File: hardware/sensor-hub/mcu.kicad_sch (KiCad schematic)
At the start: 44 parts, among them J1 Conn_ARM_JTAG_SWD_10, J2 Micro_SD_Card_Det2, SW1 SW_Push, U1 STM32F411CEUx, U4 PCAL6408ABS, Y2 32.768kHz, Y3 16MHz

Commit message: Add sensors, connectors
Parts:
- removed TP1, TP3: TestPoint, symbol Connector:TestPoint
- added J8: Conn_01x03, symbol Connector_Generic:Conn_01x03
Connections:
- net GND: now also J8.3 (Pin_3)
- net USART2_RX: now also J8.2 (Pin_2)
- net USART2_TX: now also J8.1 (Pin_1)
- net RADIO_CE: now reaches U1.10 (PA0)
- net RADIO_IRQ: now reaches U1.27 (PB14)
- net I2C1_SCL renamed SCL
- net I2C1_SDA renamed SDA
- net SPI4_MISO renamed RADIO_MISO
- net SPI4_MOSI renamed RADIO_MOSI
- net SPI4_NSS renamed RADIO_CS
- net SPI4_SCK renamed RADIO_SCK

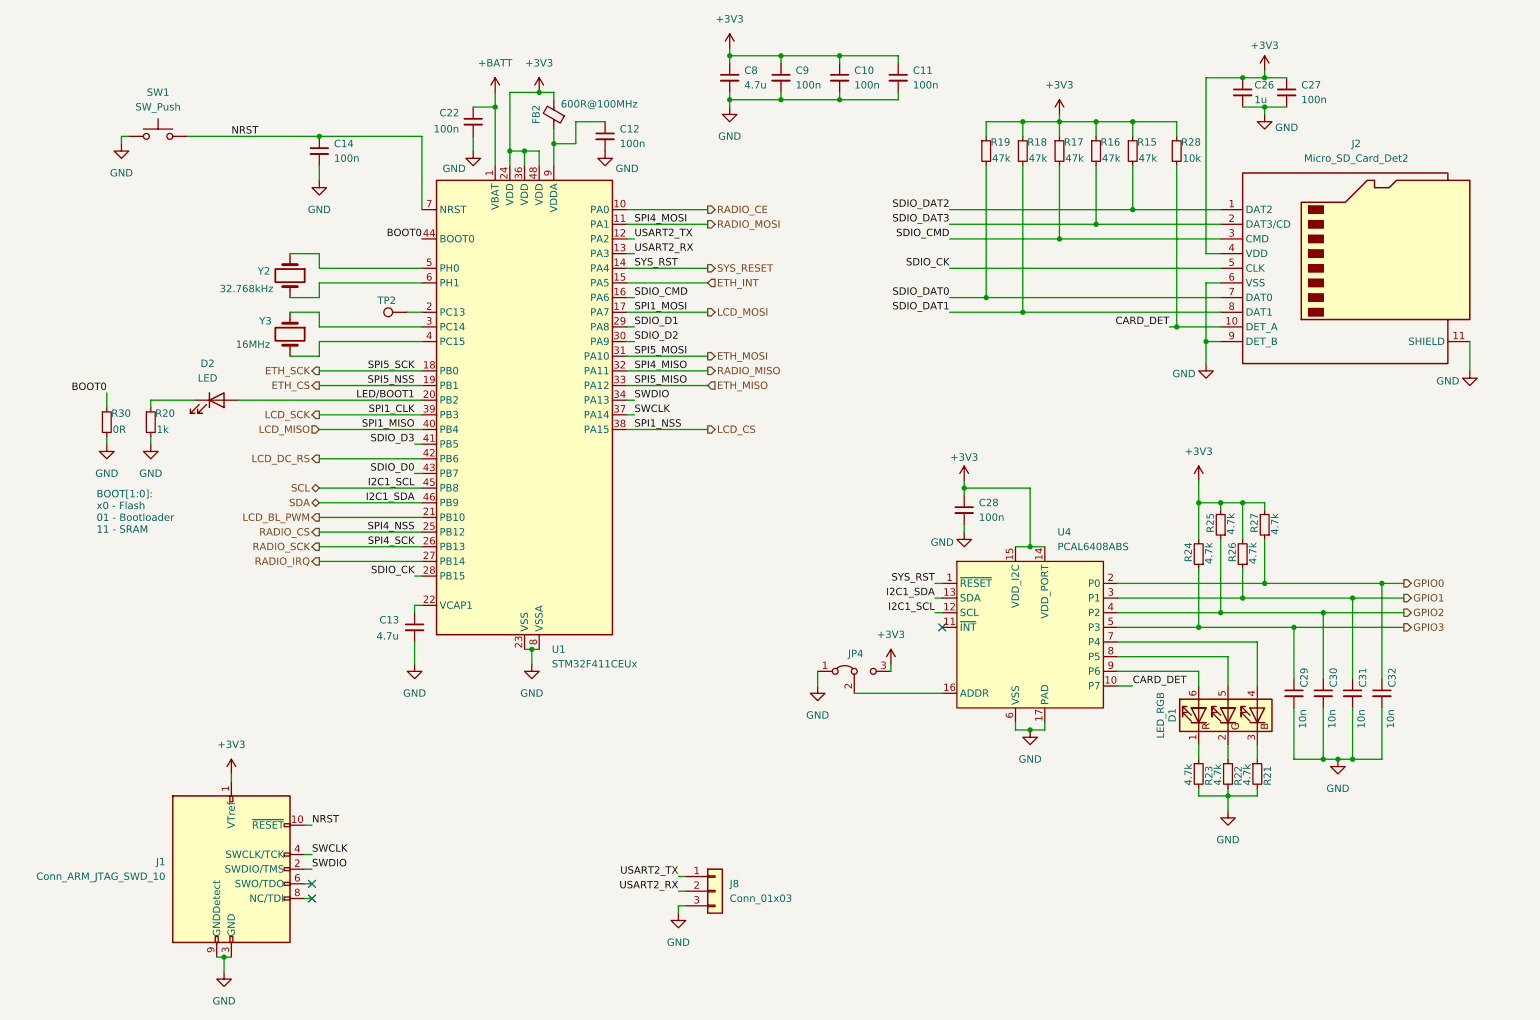
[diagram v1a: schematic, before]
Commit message: Change crystal packages, assign footprints
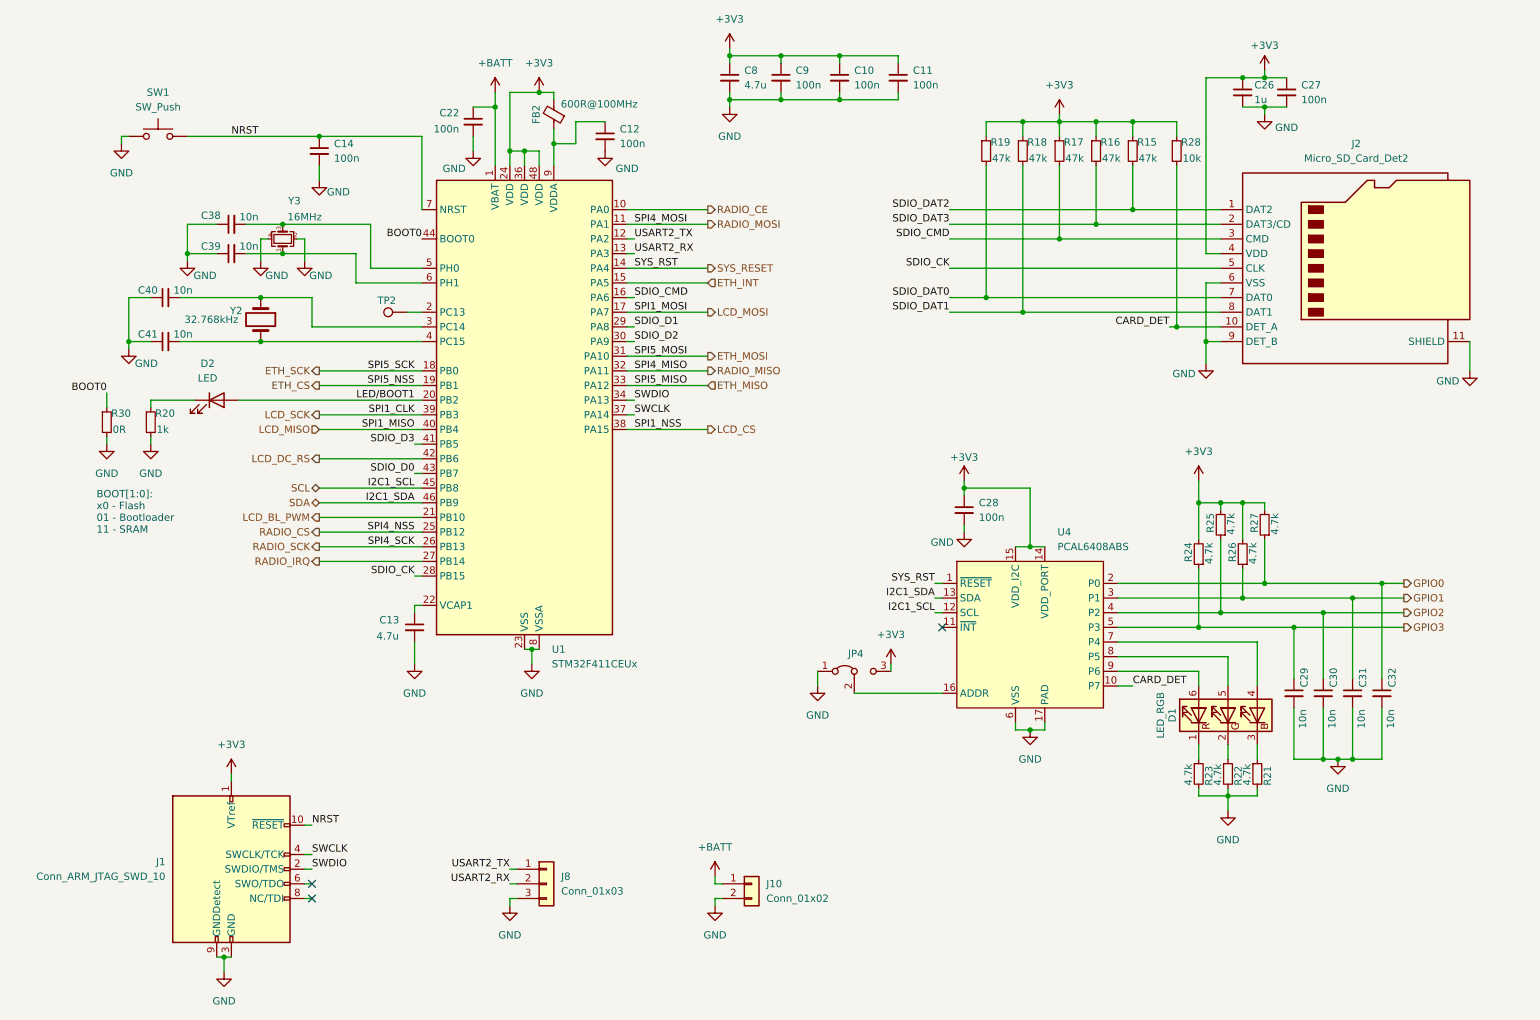
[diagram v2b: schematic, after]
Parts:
- removed Y3: 16MHz, symbol Device:Crystal
- added C38, C39, C40, C41: 10n, Capacitor_SMD:C_0603_1608Metric, symbol Device:C_Small
- added J10: Conn_01x02, Battery:BatteryHolder_MYOUNG_BS-07-A1BJ001_CR2032, symbol Connector_Generic:Conn_01x02
- added Y3: 16MHz, symbol Device:Crystal_GND24_Small
- C10, C11, C12, C13, C14, C22, C26, C27, C28, C29, C30, C31, C32, C8, C9: footprint (none) -> Capacitor_SMD:C_0603_1608Metric
- D2: footprint (none) -> LED_SMD:LED_0603_1608Metric
- FB2: footprint (none) -> Inductor_SMD:L_0603_1608Metric
- J1: footprint (none) -> Connector_PinHeader_1.27mm:PinHeader_2x05_P1.27mm_Vertical_SMD
- J2: footprint (none) -> sensor-hub-footprints:MicroSD_Det2
- J8: footprint (none) -> Connector_PinHeader_2.54mm:PinHeader_1x03_P2.54mm_Vertical
- JP4: footprint (none) -> Jumper:SolderJumper-3_P1.3mm_Bridged12_RoundedPad1.0x1.5mm
- R15, R16, R17, R18, R19, R20, R21, R22, R23, R24, R25, R26, R27, R28, R30: footprint (none) -> Resistor_SMD:R_0603_1608Metric
- SW1: footprint (none) -> Button_Switch_SMD:SW_SPST_CK_RS282G05A3
- TP2: footprint (none) -> TestPoint:TestPoint_Pad_D1.0mm
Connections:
- net +BATT: now also J10.1 (Pin_1)
- net GND: now also C38.1, C39.1, C40.1, C41.1, J10.2 (Pin_2), Y3.2, Y3.4
- net at U1.5 (PH0): now also C38.2, Y3.3; no longer Y2.1
- net at Y2.2: now also U1.4 (PC15), C41.2; no longer U1.6 (PH1)
- net at U1.3 (PC14): now also Y2.1, C40.2
- new net: C39.2, U1.6 (PH1), Y3.1
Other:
- moved on the sheet: J8, Y2

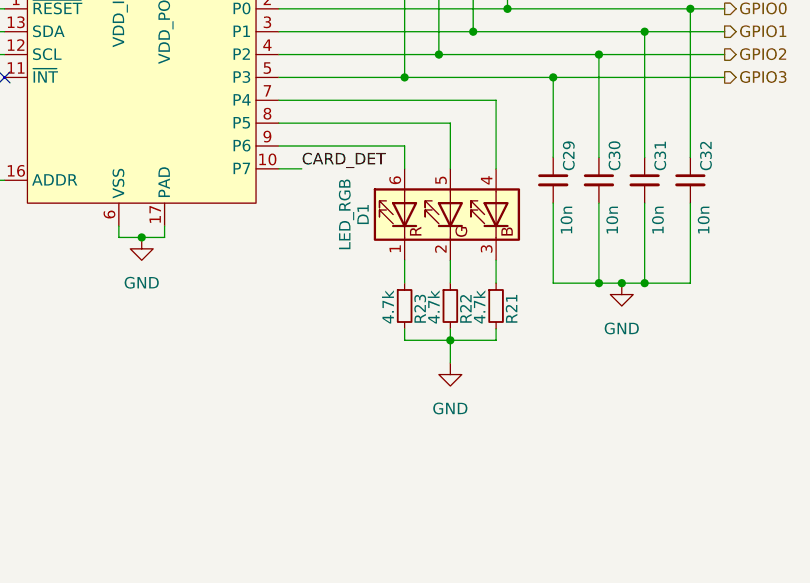
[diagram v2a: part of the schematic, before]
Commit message: Assign remaining footprints, change HT sensor
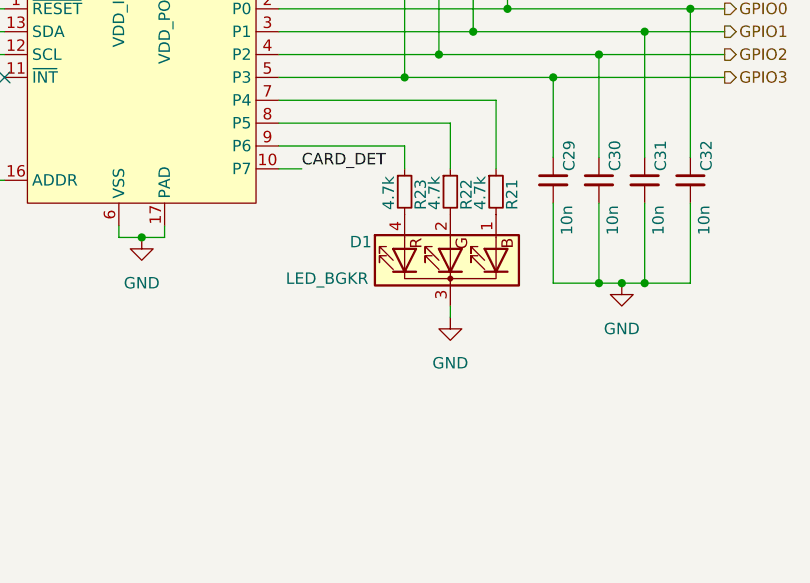
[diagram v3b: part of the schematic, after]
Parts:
- removed D1: LED_RGB, symbol Device:LED_RGB
- added D1: LED_BGKR, LED_SMD:LED_Cree-PLCC4_3.2x2.8mm_CCW, symbol Device:LED_BGKR
- Y2: footprint (none) -> Crystal:Crystal_SMD_3215-2Pin_3.2x1.5mm
- Y3: footprint (none) -> Crystal:Crystal_SMD_SeikoEpson_TSX3225-4Pin_3.2x2.5mm
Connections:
- net GND: now also D1.3 (K); no longer R21.2, R22.2, R23.2
- net at U4.7 (P4): now also R21.1
- net at U4.8 (P5): now also R22.1
- net at U4.9 (P6): now also R23.1
- new net: D1.2 (GA), R22.2
- new net: D1.4 (RA), R23.2
- new net: D1.1 (BA), R21.2
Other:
- moved on the sheet: R21, R22, R23
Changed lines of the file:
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@@
 	)
 	(junction
-		(at 227.33 152.4)
-		(diameter 0)
-		(color 0 0 0 0)
-	)
-	(junction
 		(at 218.44 71.12)
 		(diameter 0)
@@
 	(wire
 		(pts
-			(xy 227.33 152.4) (xy 232.41 152.4)
-		)
-		(stroke
-			(width 0)
-			(type default)
-		)
-	)
-	(wire
-		(pts
 			(xy 208.28 123.19) (xy 222.25 123.19)
 		)
@@
 	(wire
 		(pts
-			(xy 227.33 152.4) (xy 227.33 154.94)
-		)
-		(stroke
-			(width 0)
-			(type default)
-		)
-	)
-	(wire
-		(pts
-			(xy 222.25 143.51) (xy 222.25 146.05)
-		)
-		(stroke
-			(width 0)
-			(type default)
-		)
-	)
-	(wire
-		(pts
 			(xy 248.92 118.11) (xy 248.92 132.08)
 		)
@@
 	(wire
 		(pts
+			(xy 227.33 148.59) (xy 227.33 149.86)
+		)
+		(stroke
+			(width 0)
+			(type default)
+		)
+	)
+	(wire
+		(pts
 			(xy 107.95 40.64) (xy 105.41 40.64)
 		)
@@
 	(wire
 		(pts
-			(xy 222.25 151.13) (xy 222.25 152.4)
-		)
-		(stroke
-			(width 0)
-			(type default)
-		)
-	)
-	(wire
-		(pts
 			(xy 243.84 120.65) (xy 257.81 120.65)
 		)
@@
 	(wire
 		(pts
-			(xy 232.41 151.13) (xy 232.41 152.4)
-		)
-		(stroke
-			(width 0)
-			(type default)
-		)
-	)
-	(wire
-		(pts
 			(xy 190.5 109.22) (xy 193.04 109.22)
 		)
@@
 	(wire
 		(pts
-			(xy 222.25 152.4) (xy 227.33 152.4)
-		)
-		(stroke
-			(width 0)
-			(type default)
-		)
-	)
-	(wire
-		(pts
 			(xy 181.61 97.79) (xy 181.61 99.06)
 		)
@@
 	(wire
 		(pts
-			(xy 232.41 143.51) (xy 232.41 146.05)
-		)
-		(stroke
-			(width 0)
-			(type default)
-		)
-	)
-	(wire
-		(pts
 			(xy 105.41 40.64) (xy 102.87 40.64)
 		)
@@
 	(wire
 		(pts
-			(xy 227.33 143.51) (xy 227.33 146.05)
-		)
-		(stroke
-			(width 0)
-			(type default)
-		)
-	)
-	(wire
-		(pts
 			(xy 181.61 105.41) (xy 181.61 106.68)
 		)
@@
 	(wire
 		(pts
-			(xy 227.33 151.13) (xy 227.33 152.4)
-		)
-		(stroke
-			(width 0)
-			(type default)
-		)
-	)
-	(wire
-		(pts
 			(xy 222.25 97.79) (xy 222.25 101.6)
 		)
@@
 	)
 	(symbol
-		(lib_id "Device:LED_RGB")
-		(at 227.33 138.43 90)
-		(unit 1)
-		(exclude_from_sim no)
-		(in_bom yes)
-		(on_board yes)
-		(dnp no)
-		(property "Reference" "D1"
-			(at 217.678 138.43 0)
-			(effects
-				(font
-					(size 1.27 1.27)
-				)
-			)
-		)
-		(property "Value" "LED_RGB"
-			(at 215.646 138.43 0)
-			(effects
-				(font
-					(size 1.27 1.27)
-				)
-			)
-		)
-		(property "Footprint" ""
-			(at 228.6 138.43 0)
-			(effects
-				(font
-					(size 1.27 1.27)
-				)
-				(hide yes)
-			)
-		)
-		(property "Datasheet" "~"
-			(at 228.6 138.43 0)
-			(effects
-				(font
-					(size 1.27 1.27)
-				)
-				(hide yes)
-			)
-		)
-		(property "Description" "RGB LED, 6 pin package"
-			(at 227.33 138.43 0)
-			(effects
-				(font
-					(size 1.27 1.27)
-				)
-				(hide yes)
-			)
-		)
-		(pin "4"
-		)
-		(pin "6"
-		)
-		(pin "1"
-		)
-		(pin "2"
-		)
-		(pin "3"
-		)
-		(pin "5"
-		)
-		(instances
-			(project ""
-				(path "/e168ef7b-16e4-493f-b63c-2f69374fc890/acb07f68-122e-4e37-938b-04e6ced67923"
-					(reference "D1")
-					(unit 1)
-				)
-			)
-		)
-	)
-	(symbol
 		(lib_id "Device:R_Small")
 		(at 185.42 40.64 0)
@@
 			)
 		)
-		(property "Footprint" ""
+		(property "Footprint" "Crystal:Crystal_SMD_3215-2Pin_3.2x1.5mm"
 			(at 59.69 69.85 0)
 			(effects
@@
 	(symbol
 		(lib_id "Device:R_Small")
-		(at 227.33 148.59 0)
+		(at 227.33 135.89 0)
 		(unit 1)
 		(exclude_from_sim no)
@@
 		(dnp no)
 		(property "Reference" "R22"
-			(at 229.108 150.622 90)
+			(at 229.108 137.922 90)
 			(effects
 				(font
@@
 		)
 		(property "Value" "4.7k"
-			(at 225.552 150.622 90)
+			(at 225.552 137.922 90)
 			(effects
 				(font
@@
 		)
 		(property "Footprint" "Resistor_SMD:R_0603_1608Metric"
-			(at 227.33 148.59 0)
+			(at 227.33 135.89 0)
 			(effects
 				(font
@@
 		)
 		(property "Datasheet" "~"
-			(at 227.33 148.59 0)
+			(at 227.33 135.89 0)
 			(effects
 				(font
@@
 		)
 		(property "Description" "Resistor, small symbol"
-			(at 227.33 148.59 0)
+			(at 227.33 135.89 0)
 			(effects
 				(font
@@
 	(symbol
 		(lib_id "power:GND")
-		(at 227.33 154.94 0)
+		(at 227.33 149.86 0)
 		(unit 1)
 		(exclude_from_sim no)
@@
 		(fields_autoplaced yes)
 		(property "Reference" "#PWR54"
-			(at 227.33 161.29 0)
+			(at 227.33 156.21 0)
 			(effects
 				(font
@@
 		)
 		(property "Value" "GND"
-			(at 227.33 160.02 0)
+			(at 227.33 154.94 0)
 			(effects
 				(font
@@
 		)
 		(property "Footprint" ""
-			(at 227.33 154.94 0)
+			(at 227.33 149.86 0)
 			(effects
 				(font
@@
 		)
 		(property "Datasheet" ""
-			(at 227.33 154.94 0)
+			(at 227.33 149.86 0)
 			(effects
 				(font
@@
 		)
 		(property "Description" "Power symbol creates a global label with name \"GND\" , ground"
-			(at 227.33 154.94 0)
+			(at 227.33 149.86 0)
 			(effects
 				(font
@@
 	(symbol
 		(lib_id "Device:R_Small")
-		(at 222.25 148.59 0)
+		(at 222.25 135.89 0)
 		(unit 1)
 		(exclude_from_sim no)
@@
 		(dnp no)
 		(property "Reference" "R23"
-			(at 224.028 150.622 90)
+			(at 224.028 137.922 90)
 			(effects
 				(font
@@
 		)
 		(property "Value" "4.7k"
-			(at 220.472 150.622 90)
+			(at 220.472 137.922 90)
 			(effects
 				(font
@@
 		)
 		(property "Footprint" "Resistor_SMD:R_0603_1608Metric"
-			(at 222.25 148.59 0)
+			(at 222.25 135.89 0)
 			(effects
 				(font
@@
 		)
 		(property "Datasheet" "~"
-			(at 222.25 148.59 0)
+			(at 222.25 135.89 0)
 			(effects
 				(font
@@
 		)
 		(property "Description" "Resistor, small symbol"
-			(at 222.25 148.59 0)
+			(at 222.25 135.89 0)
 			(effects
 				(font
@@
 	)
 	(symbol
+		(lib_id "Device:LED_BGKR")
+		(at 227.33 143.51 90)
+		(unit 1)
+		(exclude_from_sim no)
+		(in_bom yes)
+		(on_board yes)
+		(dnp no)
+		(property "Reference" "D1"
+			(at 216.154 141.478 90)
+			(effects
+				(font
+					(size 1.27 1.27)
+				)
+				(justify right)
+			)
+		)
+		(property "Value" "LED_BGKR"
+			(at 209.042 145.542 90)
+			(effects
+				(font
+					(size 1.27 1.27)
+				)
+				(justify right)
+			)
+		)
+		(property "Footprint" "LED_SMD:LED_Cree-PLCC4_3.2x2.8mm_CCW"
+			(at 228.6 143.51 0)
+			(effects
+				(font
+					(size 1.27 1.27)
+				)
+				(hide yes)
+			)
+		)
+		(property "Datasheet" "~"
+			(at 228.6 143.51 0)
+			(effects
+				(font
+					(size 1.27 1.27)
+				)
+				(hide yes)
+			)
+		)
+		(property "Description" "RGB LED, blue/green/cathode/red"
+			(at 227.33 143.51 0)
+			(effects
+				(font
+					(size 1.27 1.27)
+				)
+				(hide yes)
+			)
+		)
+		(pin "1"
+		)
+		(pin "4"
+		)
+		(pin "2"
+		)
+		(pin "3"
+		)
+		(instances
+			(project ""
+				(path "/e168ef7b-16e4-493f-b63c-2f69374fc890/acb07f68-122e-4e37-938b-04e6ced67923"
+					(reference "D1")
+					(unit 1)
+				)
+			)
+		)
+	)
+	(symbol
 		(lib_id "power:+3V3")
 		(at 181.61 97.79 0)
@@
 	(symbol
 		(lib_id "Device:R_Small")
-		(at 232.41 148.59 0)
+		(at 232.41 135.89 0)
 		(unit 1)
 		(exclude_from_sim no)
@@
 		(dnp no)
 		(property "Reference" "R21"
-			(at 234.188 150.622 90)
+			(at 234.188 137.922 90)
 			(effects
 				(font
@@
 		)
 		(property "Value" "4.7k"
-			(at 230.632 150.622 90)
+			(at 230.632 137.922 90)
 			(effects
 				(font
@@
 		)
 		(property "Footprint" "Resistor_SMD:R_0603_1608Metric"
-			(at 232.41 148.59 0)
+			(at 232.41 135.89 0)
 			(effects
 				(font
@@
 		)
 		(property "Datasheet" "~"
-			(at 232.41 148.59 0)
+			(at 232.41 135.89 0)
 			(effects
 				(font
@@
 		)
 		(property "Description" "Resistor, small symbol"
-			(at 232.41 148.59 0)
+			(at 232.41 135.89 0)
 			(effects
 				(font
@@
 			)
 		)
-		(property "Footprint" ""
+		(property "Footprint" "Crystal:Crystal_SMD_SeikoEpson_TSX3225-4Pin_3.2x2.5mm"
 			(at 63.5 55.88 0)
 			(effects

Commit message: Start layout
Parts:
- J10: value Conn_01x02 -> BATT
- J8: value Conn_01x03 -> UART_CONN
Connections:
- net SDIO_D0 is gone; now on net SDIO_DAT0: U1.43 (PB7)
- net SDIO_D1 is gone; now on net SDIO_DAT1: U1.29 (PA8)
- net SDIO_D2 is gone; now on net SDIO_DAT2: U1.30 (PA9)
- net SDIO_D3 is gone; now on net SDIO_DAT3: U1.41 (PB5)
- net +3V3 renamed +3.3V
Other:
- note added: "HSE, LSE load caps Cc = 2(Cl-Cs), per ST AN2867 (Cs:3-5pF) LSE: 9pF Cl, Cc=2(9pF-Cs) = 8-12pF HSE: 18pF Cl, Cc=2(18pF-Cs) = 26-30pF 12pF Cl, Cc=2(12pF-Cs) = 14-18pF"
